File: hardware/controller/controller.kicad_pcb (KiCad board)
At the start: 2 copper layers, 100 x 100 mm, 133 parts, among them J1 230V~, J10 FAN, J2 LOAD, J3 DISPLAY, J4 PANEL, J5 TC top, J6 TC bot, J7 USB-C, J9 UART, Q1 AO3401A, Q2 BSS138, Q3 IRLML6346, Q4 IRLML6346, Q5 IRLML6346, Q6 AO3401A, Q7 IRLML6346, Q8 BSS138, SW1 RESET, SW2 BOOT, U1 IRM-10-5, U10 USBLC6-2SC6, U11 USBLC6-2SC6, U12 USBLC6-2SC6, U2 AP7361C-33E, U3 ESP32-S3-WROOM-1U-N8, U4 USBLC6-2SC6, U5 MAX31856MUD+, U6 MAX31856MUD+, U7 SN74LVC74AD, U8 TPS3828-33DBV, U9 TC6501P065

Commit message: feat(hardware): sheet cleanup done, ERC clean (T071)
- Leistung/Steuerung sheets cleaned up and readable, intersheet references on
- embedded symbols updated from the libraries (lib_symbol_mismatch gone)
- stray and off-grid wire stubs removed
- PWR_FLAGs on N_IN, L_FUSED, +5V and VBUS
- ERC exclusion for the shared SDO line of U5/U6 (MAX31856, tristate)
- PCB nets re-imported, U7 relinked

kicad-cli ERC: 0 violations, check_schematic: 0 errors, parity DRC clean.

Co-Authored-By: Claude Opus 5.5 <noreply@anthropic.com>
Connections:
- net /Steuerung und Messung/ENC_A_RAW renamed Net-(J4-Pin_1)
- net /Steuerung und Messung/ENC_B_RAW renamed Net-(J4-Pin_3)
- net /Steuerung und Messung/ENC_SW_RAW renamed Net-(J4-Pin_4)
- net /Steuerung und Messung/STOP_NO_RAW renamed Net-(J4-Pin_7)
- net BUZZER_G renamed /Steuerung und Messung/BUZZER_G
- net HEAT_BOT_G renamed Net-(Q4-G)
- net HEAT_TOP_G renamed Net-(Q3-G)
- net LATCH_Q_G renamed Net-(Q5-G)
- net SSR_EN_N renamed Net-(Q1-G)
- net STOP_NC_OUT renamed Net-(J4-Pin_5)
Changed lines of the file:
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@@
 			(layers "F.Cu" "F.Mask" "F.Paste")
 			(roundrect_rratio 0.25)
-			(net "/Steuerung und Messung/STOP_NO_RAW")
+			(net "Net-(J4-Pin_7)")
 		)
 		(pad "2" smd roundrect
@@
 			(layers "F.Cu" "F.Mask" "F.Paste")
 			(roundrect_rratio 0.25)
-			(net "/Steuerung und Messung/STOP_NO_RAW")
+			(net "Net-(J4-Pin_7)")
 		)
 		(embedded_fonts no)
@@
 			(layers "F.Cu" "F.Mask" "F.Paste")
 			(roundrect_rratio 0.25)
-			(net "/Steuerung und Messung/ENC_SW_RAW")
+			(net "Net-(J4-Pin_4)")
 		)
 		(embedded_fonts no)
@@
 			(layers "F.Cu" "F.Mask" "F.Paste")
 			(roundrect_rratio 0.25)
-			(net "LATCH_Q_G")
+			(net "Net-(Q5-G)")
 		)
 		(pad "2" smd roundrect
@@
 			(layers "F.Cu" "F.Mask" "F.Paste")
 			(roundrect_rratio 0.25)
-			(net "HEAT_BOT_G")
+			(net "Net-(Q4-G)")
 		)
 		(pad "2" smd roundrect
@@
 			(layers "F.Cu" "F.Mask" "F.Paste")
 			(roundrect_rratio 0.25)
-			(net "LATCH_Q_G")
+			(net "Net-(Q5-G)")
 		)
 		(pad "2" smd roundrect
@@
 			(layers "F.Cu" "F.Mask" "F.Paste")
 			(roundrect_rratio 0.25)
-			(net "HEAT_TOP_G")
+			(net "Net-(Q3-G)")
 		)
 		(pad "2" smd roundrect
@@
 			(layers "F.Cu" "F.Mask" "F.Paste")
 			(roundrect_rratio 0.25)
-			(net "STOP_NC_OUT")
+			(net "Net-(J4-Pin_5)")
 		)
 		(pad "2" smd roundrect
@@
 			(layers "F.Cu" "F.Mask" "F.Paste")
 			(roundrect_rratio 0.25)
-			(net "STOP_NC_OUT")
+			(net "Net-(J4-Pin_5)")
 		)
 		(embedded_fonts no)
@@
 			(layers "F.Cu" "F.Mask" "F.Paste")
 			(roundrect_rratio 0.25)
-			(net "BUZZER_G")
+			(net "/Steuerung und Messung/BUZZER_G")
 		)
 		(pad "2" smd roundrect
@@
 			(layers "F.Cu" "F.Mask" "F.Paste")
 			(roundrect_rratio 0.25)
-			(net "/Steuerung und Messung/ENC_B_RAW")
+			(net "Net-(J4-Pin_3)")
 		)
 		(pad "2" smd roundrect
@@
 			(layers "F.Cu" "F.Mask" "F.Paste")
 			(roundrect_rratio 0.25)
-			(net "SSR_EN_N")
+			(net "Net-(Q1-G)")
 		)
 		(embedded_fonts no)
@@
 			(layers "F.Cu" "F.Mask" "F.Paste")
 			(roundrect_rratio 0.25)
-			(net "/Steuerung und Messung/ENC_A_RAW")
+			(net "Net-(J4-Pin_1)")
 		)
 		(pad "2" smd roundrect
@@
 			(layers "F.Cu" "F.Mask" "F.Paste")
 			(roundrect_rratio 0.25)
-			(net "/Steuerung und Messung/ENC_B_RAW")
+			(net "Net-(J4-Pin_3)")
 		)
 		(pad "4" smd roundrect
@@
 			(layers "F.Cu" "F.Mask" "F.Paste")
 			(roundrect_rratio 0.25)
-			(net "/Steuerung und Messung/ENC_B_RAW")
+			(net "Net-(J4-Pin_3)")
 		)
 		(pad "5" smd roundrect
@@
 			(layers "F.Cu" "F.Mask" "F.Paste")
 			(roundrect_rratio 0.25)
-			(net "/Steuerung und Messung/ENC_A_RAW")
+			(net "Net-(J4-Pin_1)")
 		)
 		(embedded_fonts no)
@@
 			(layers "F.Cu" "F.Mask" "F.Paste")
 			(roundrect_rratio 0.25)
-			(net "/Steuerung und Messung/ENC_SW_RAW")
+			(net "Net-(J4-Pin_4)")
 		)
 		(pad "2" smd roundrect
@@
 			(layers "F.Cu" "F.Mask" "F.Paste")
 			(roundrect_rratio 0.25)
-			(net "HEAT_BOT_G")
+			(net "Net-(Q4-G)")
 		)
 		(pad "2" smd roundrect
@@
 			(layers "F.Cu" "F.Mask" "F.Paste")
 			(roundrect_rratio 0.25)
-			(net "HEAT_TOP_G")
+			(net "Net-(Q3-G)")
 		)
 		(embedded_fonts no)
@@
 			(remove_unused_layers no)
 			(roundrect_rratio 0.147059)
-			(net "/Steuerung und Messung/ENC_A_RAW")
+			(net "Net-(J4-Pin_1)")
 		)
 		(pad "2" thru_hole circle
@@
 			(layers "*.Cu" "*.Mask")
 			(remove_unused_layers no)
-			(net "/Steuerung und Messung/ENC_B_RAW")
+			(net "Net-(J4-Pin_3)")
 		)
 		(pad "4" thru_hole circle
@@
 			(layers "*.Cu" "*.Mask")
 			(remove_unused_layers no)
-			(net "/Steuerung und Messung/ENC_SW_RAW")
+			(net "Net-(J4-Pin_4)")
 		)
 		(pad "5" thru_hole circle
@@
 			(layers "*.Cu" "*.Mask")
 			(remove_unused_layers no)
-			(net "STOP_NC_OUT")
+			(net "Net-(J4-Pin_5)")
 		)
 		(pad "6" thru_hole circle
@@
 			(layers "*.Cu" "*.Mask")
 			(remove_unused_layers no)
-			(net "/Steuerung und Messung/STOP_NO_RAW")
+			(net "Net-(J4-Pin_7)")
 		)
 		(pad "8" thru_hole circle
@@
 			(layers "F.Cu" "F.Mask" "F.Paste")
 			(roundrect_rratio 0.25)
-			(net "BUZZER_G")
+			(net "/Steuerung und Messung/BUZZER_G")
 		)
 		(pad "2" smd roundrect
@@
 			(layers "F.Cu" "F.Mask" "F.Paste")
 			(roundrect_rratio 0.25)
-			(net "HEAT_BOT_G")
+			(net "Net-(Q4-G)")
 		)
 		(embedded_fonts no)
@@
 			(layers "F.Cu" "F.Mask" "F.Paste")
 			(roundrect_rratio 0.25)
-			(net "BUZZER_G")
+			(net "/Steuerung und Messung/BUZZER_G")
 		)
 		(embedded_fonts no)
@@
 			(layers "F.Cu" "F.Mask" "F.Paste")
 			(roundrect_rratio 0.25)
-			(net "/Steuerung und Messung/ENC_A_RAW")
+			(net "Net-(J4-Pin_1)")
 		)
 		(pad "2" smd roundrect
@@
 			(layers "F.Cu" "F.Mask" "F.Paste")
 			(roundrect_rratio 0.25)
-			(net "STOP_NC_OUT")
+			(net "Net-(J4-Pin_5)")
 		)
 		(embedded_fonts no)
@@
 			(layers "F.Cu" "F.Mask" "F.Paste")
 			(roundrect_rratio 0.25)
-			(net "HEAT_TOP_G")
+			(net "Net-(Q3-G)")
 		)
 		(pad "2" smd roundrect
@@
 			(layers "F.Cu" "F.Mask" "F.Paste")
 			(roundrect_rratio 0.25)
-			(net "LATCH_Q_G")
+			(net "Net-(Q5-G)")
 		)
 		(embedded_fonts no)
@@
 			(layers "F.Cu" "F.Mask" "F.Paste")
 			(roundrect_rratio 0.25)
-			(net "SSR_EN_N")
+			(net "Net-(Q1-G)")
 		)
 		(pad "2" smd roundrect
@@
 			(layers "F.Cu" "F.Mask" "F.Paste")
 			(roundrect_rratio 0.25)
-			(net "/Steuerung und Messung/ENC_B_RAW")
+			(net "Net-(J4-Pin_3)")
 		)
 		(embedded_fonts no)
@@
 			(layers "F.Cu" "F.Mask" "F.Paste")
 			(roundrect_rratio 0.25)
-			(net "SSR_EN_N")
+			(net "Net-(Q1-G)")
 		)
 		(embedded_fonts no)
@@
 			(layers "F.Cu" "F.Mask" "F.Paste")
 			(roundrect_rratio 0.25)
-			(net "/Steuerung und Messung/ENC_SW_RAW")
+			(net "Net-(J4-Pin_4)")
 		)
 		(pad "2" smd roundrect
@@
 			(layers "F.Cu" "F.Mask" "F.Paste")
 			(roundrect_rratio 0.25)
-			(net "/Steuerung und Messung/STOP_NO_RAW")
+			(net "Net-(J4-Pin_7)")
 		)
 		(pad "4" smd roundrect
@@
 			(layers "F.Cu" "F.Mask" "F.Paste")
 			(roundrect_rratio 0.25)
-			(net "/Steuerung und Messung/STOP_NO_RAW")
+			(net "Net-(J4-Pin_7)")
 		)
 		(pad "5" smd roundrect
@@
 			(layers "F.Cu" "F.Mask" "F.Paste")
 			(roundrect_rratio 0.25)
-			(net "/Steuerung und Messung/ENC_SW_RAW")
+			(net "Net-(J4-Pin_4)")
 		)
 		(embedded_fonts no)
@@
 			(layers "F.Cu" "F.Mask" "F.Paste")
 			(roundrect_rratio 0.25)
-			(net "/Steuerung und Messung/ENC_A_RAW")
+			(net "Net-(J4-Pin_1)")
 		)
 		(embedded_fonts no)

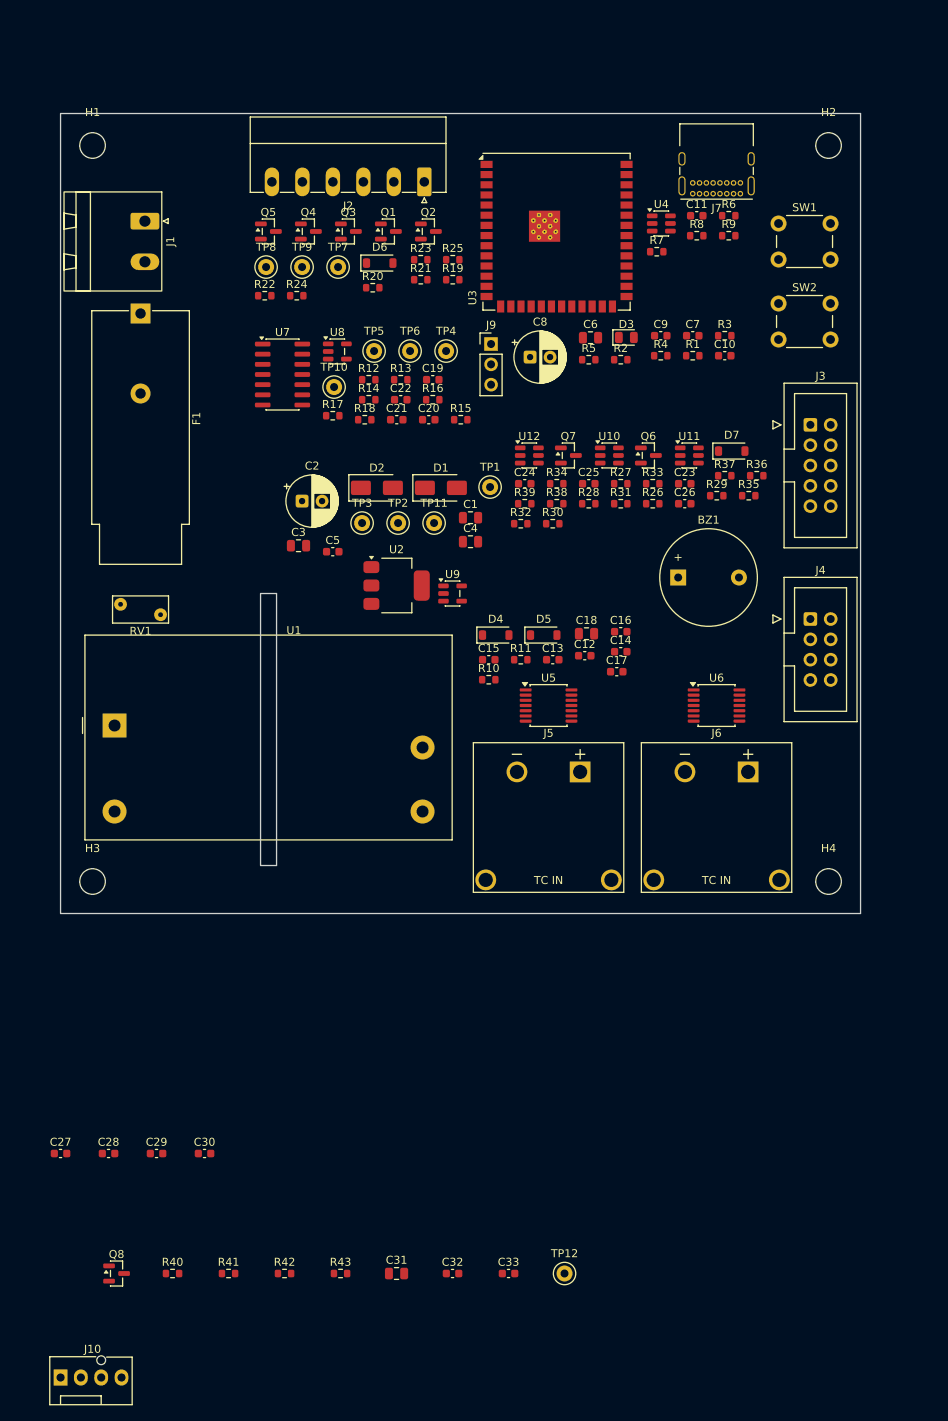
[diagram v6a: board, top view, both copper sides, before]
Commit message: feat(hardware): mains cover COV1 placed on the board (T084)
- COV1 at the board origin; H8 moved inside the cover below the IRM-10-5
  (boss on the right wall), outside its flange would block J5/J6
- J2, U2, U9, J5, J6 shifted clear of wall and flange keepouts
- thermocouple block regrouped around U5/U6 incl. input filters C27-C30
- J10 at the top edge between ESP32 module and USB-C (J7 +4 mm),
  fan circuit placed below the USB parts

DRC with schematic parity: no violations, only unconnected items and
4 silk edge warnings; check_schematic 0 errors.

Co-Authored-By: Claude Opus 5.5 <noreply@anthropic.com>
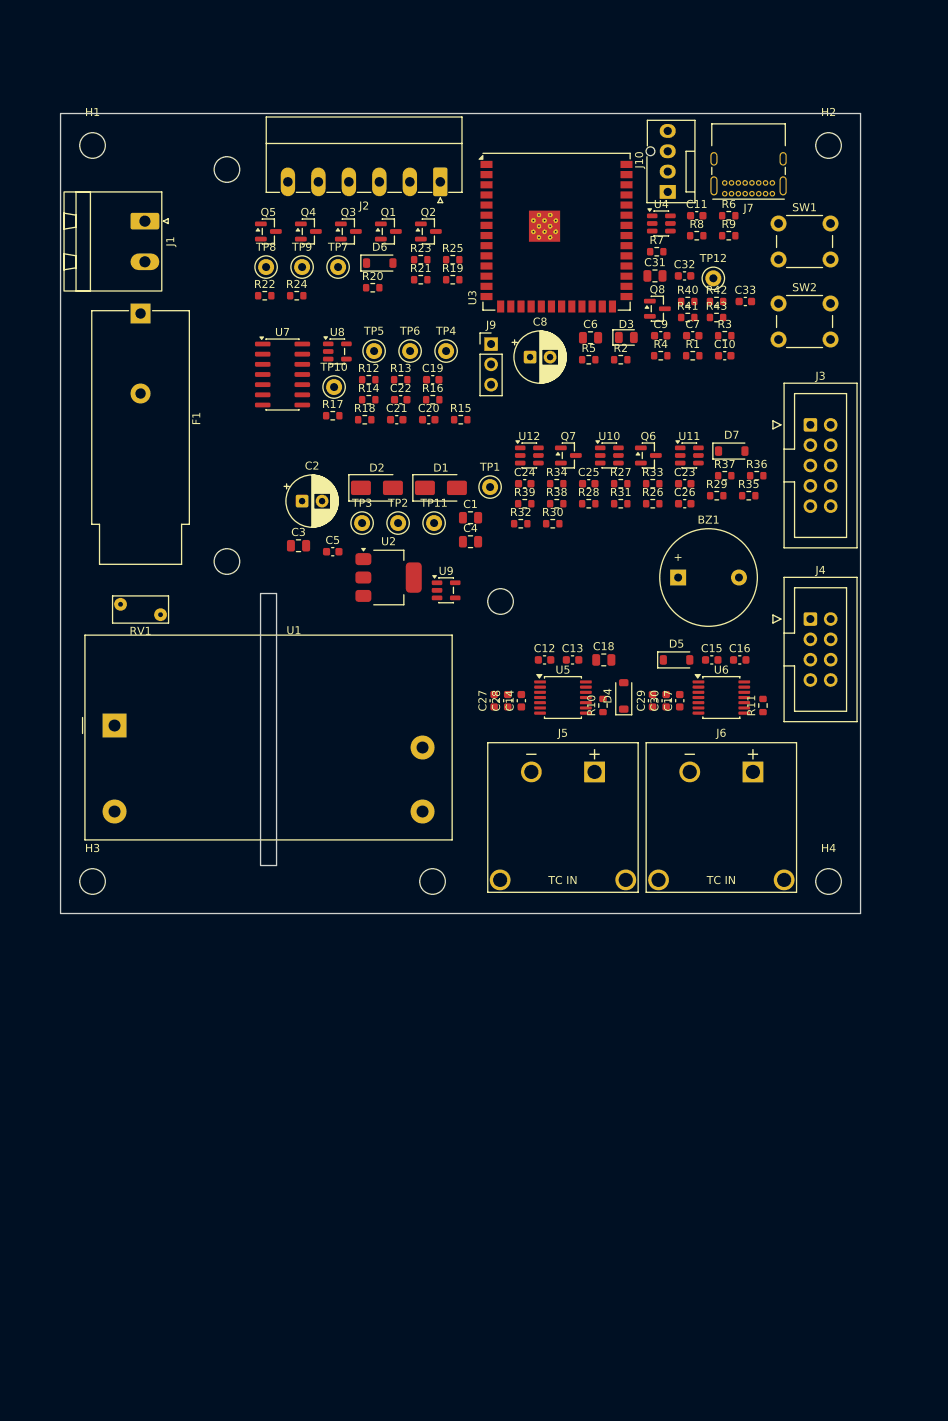
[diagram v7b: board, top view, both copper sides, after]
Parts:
- added COV1: Netzabdeckung_REVA, oven:Netzabdeckung_REVA, F.Cu at (0.00, 0.00)
- moved J10 166.5 mm to (75.9, 9.80), turned to 90 degrees
- moved Q8 138.3 mm to (74.6, 24.4)
- moved R40 137.5 mm to (78.4, 23.5)
- moved R42 133.0 mm to (82.0, 23.5)
- moved R41 132.6 mm to (78.4, 25.5)
- moved C31 128.8 mm to (74.3, 20.3)
- moved R43 128.4 mm to (82.0, 25.5)
- moved C32 128.0 mm to (78.0, 20.3)
- moved TP12 125.8 mm to (81.6, 20.6)
- moved C33 125.1 mm to (85.6, 23.5)
- moved C29 83.9 mm to (74.0, 73.4), turned to 90 degrees
- moved C30 80.8 mm to (75.7, 73.4), turned to 90 degrees
- moved C27 78.4 mm to (54.2, 73.4), turned to 90 degrees
- moved C28 75.5 mm to (55.9, 73.4), turned to 90 degrees
- moved R11 30.8 mm to (87.8, 74.0), turned to 90 degrees
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
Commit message: feat(hardware): thermocouple sockets J5/J6 switched to RS PRO 381-7564
- Omega PCC-SMP-K (46 EUR per 5-pack, dimensions only from an isometric
  drawing) replaced by RS PRO 381-7564 (type K IEC, NiCr/Ni contacts,
  about 5 EUR each, dimensioned drawing in the RS datasheet)
- new footprint oven:RS_381-7564_Horizontal: 2 pins at 7.9 mm, NPTH 2.7 mm
  for an M2.5 screw; polarity still to be checked on a sample
- schematic fields footprint/MPN/source, controller.ref.net re-exported
  (intended change; it also takes over the net names after the label
  cleanup, connectivity unchanged)
- J5/J6 swapped on the board, pins below U5/U6, 2.7 mm gap between them
- small part placement optimised for routing, silkscreen cleaned up (T020)
- value texts at U1/RV1 moved (user)
- docs and BOM updated, old Omega footprint removed

check_schematic: 0 errors, 0 notes; DRC with schematic parity: no
deviation, only unconnected items and 2 silk edge warnings at U1.

Co-Authored-By: Claude Opus 5.5 <noreply@anthropic.com>
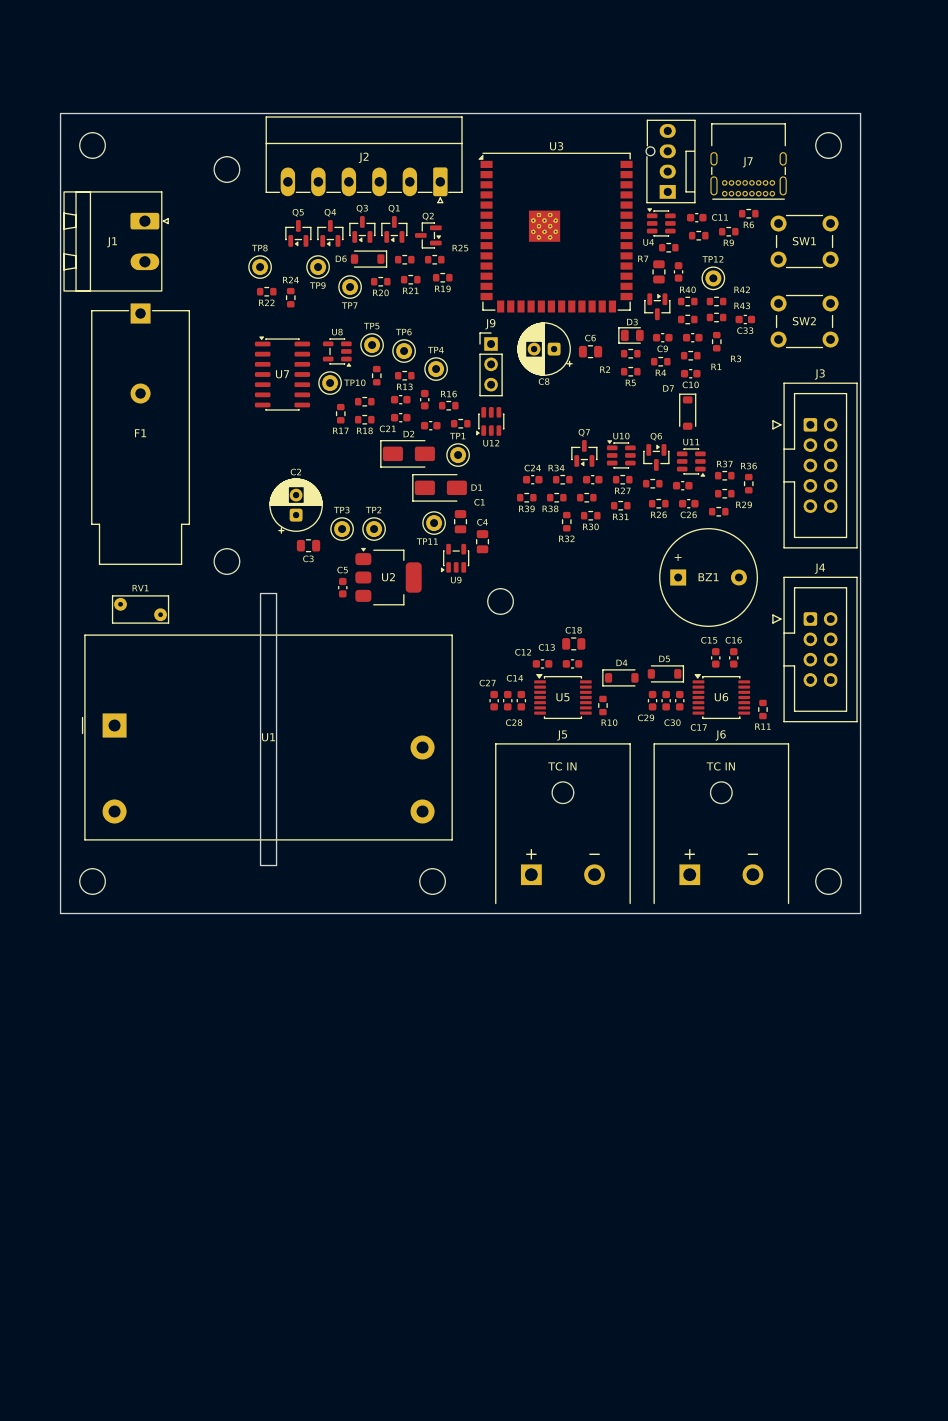
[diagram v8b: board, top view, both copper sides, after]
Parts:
- J5, J6: footprint oven:Omega_PCC-SMP_Horizontal -> oven:RS_381-7564_Horizontal
- moved D7 7.27 mm to (78.4, 37.4), turned to -90 degrees
- moved U12 6.37 mm to (53.8, 38.5), turned to 90 degrees
- moved J5 6.10 mm to (62.8, 95.2)
- moved J6 6.10 mm to (82.6, 95.2)
- moved D2 5.84 mm to (43.5, 42.5)
- moved R32 5.76 mm to (63.3, 51.0), turned to 90 degrees
- moved TP1 5.66 mm to (49.7, 42.7)
- moved R5 5.46 mm to (71.3, 32.3), turned to 180 degrees
- moved R30 4.85 mm to (66.3, 50.3)
- moved C10 4.81 mm to (78.8, 32.5)
- moved C5 4.67 mm to (35.3, 59.3), turned to 90 degrees
- moved C18 4.25 mm to (64.2, 66.3)
- moved R35 4.25 mm to (82.3, 49.8), turned to 180 degrees
- moved U9 4.19 mm to (49.5, 55.6), turned to 90 degrees
- moved Q5 3.76 mm to (29.7, 15.0), turned to 90 degrees
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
